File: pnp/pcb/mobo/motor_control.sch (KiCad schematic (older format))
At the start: 48 parts, among them J1 X_MOTOR, J2 Y_MOTOR1, J3 Z_MOTOR, J37 P_MOTOR, J38 C_MOTOR, J4 R_MOTOR, J48 Y_MOTOR2

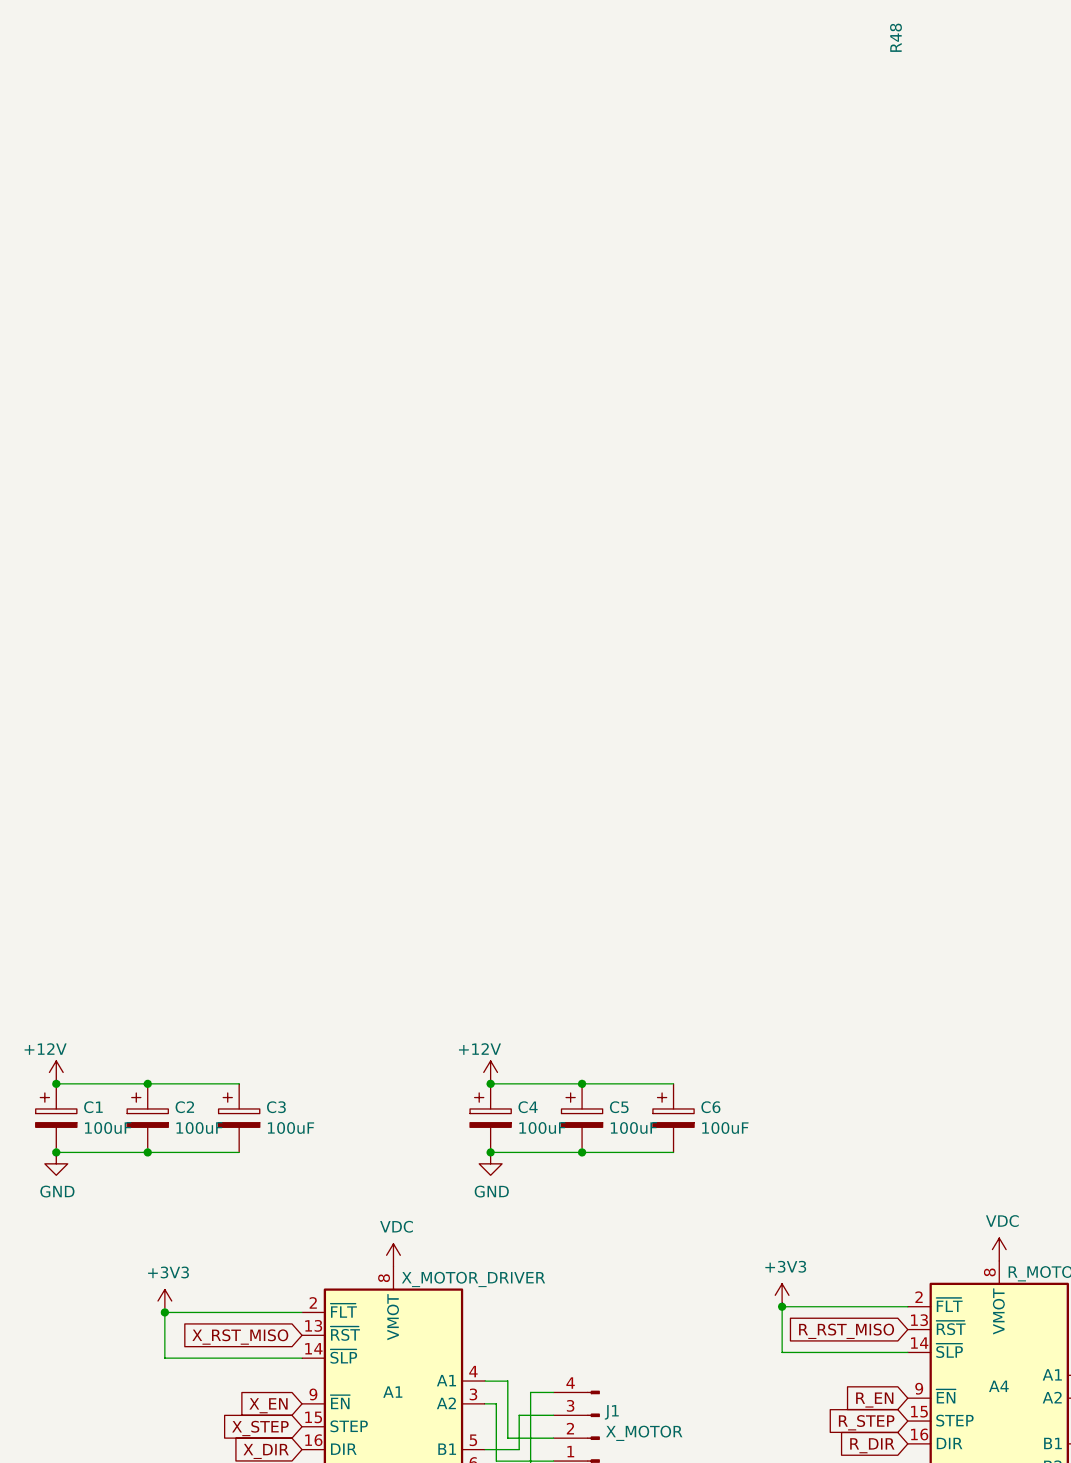
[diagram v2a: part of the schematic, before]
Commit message: Replace MOSFETs and organized vacuum sensor
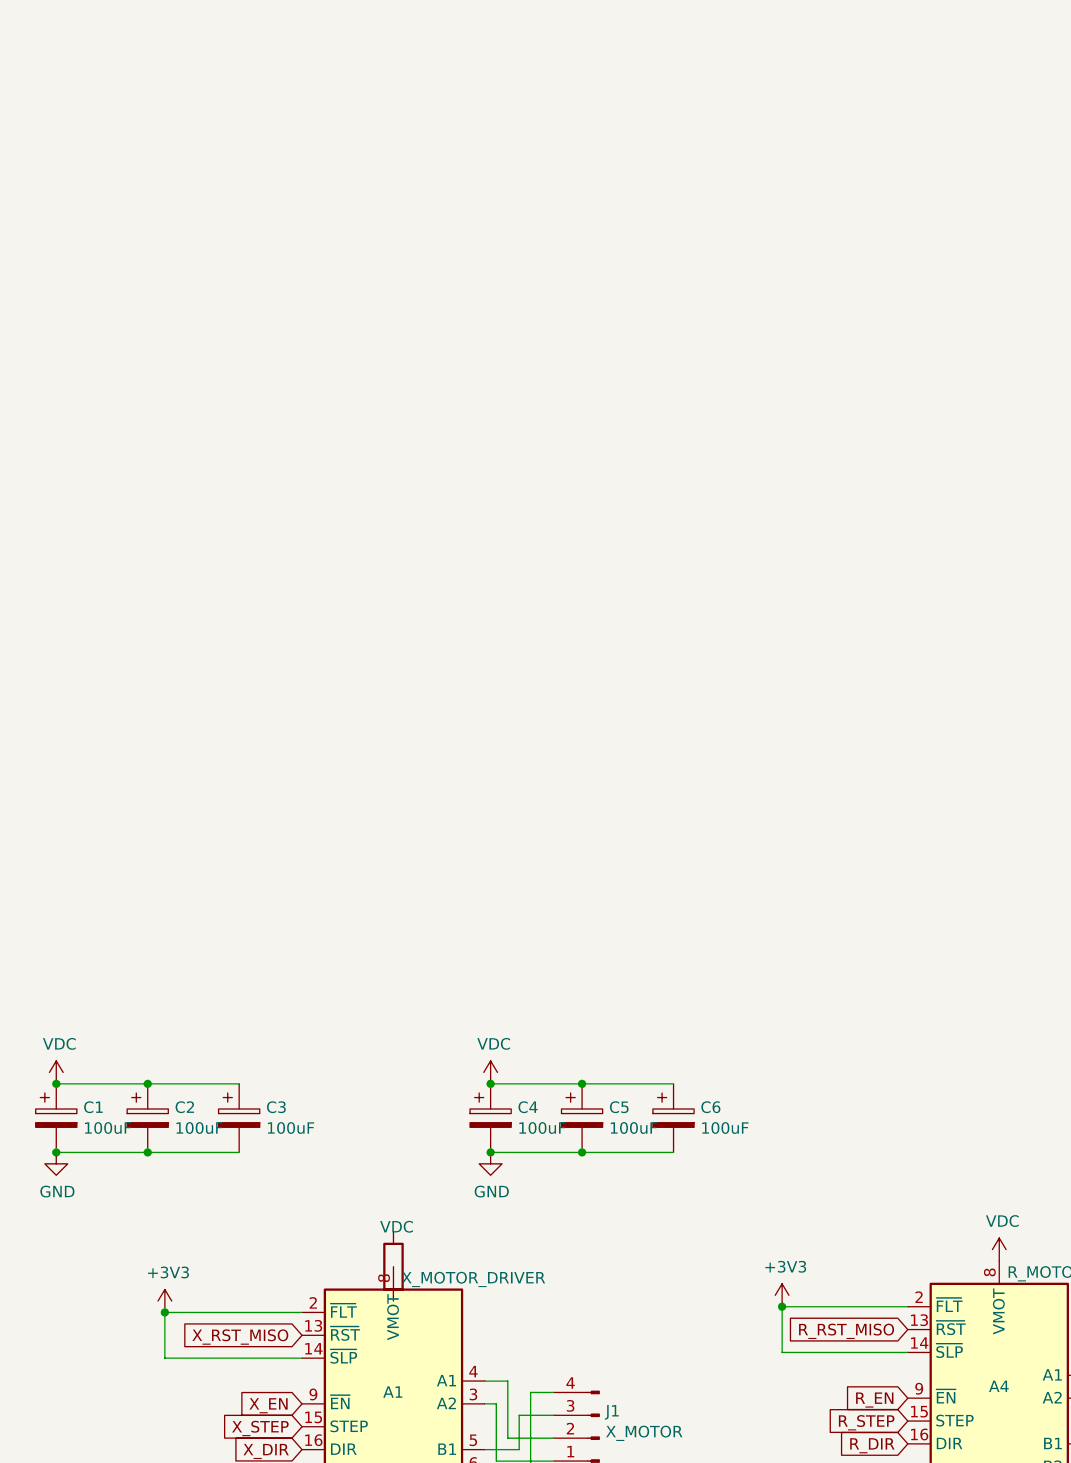
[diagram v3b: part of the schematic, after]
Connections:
- net +12V is gone; now on net VDC: C1.1, C2.1, C3.1, C4.1, C5.1, C6.1
- net VDC: no longer A1.8 (VMOT)
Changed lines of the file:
@@
 $Descr A4 11693 8268
 encoding utf-8
-Sheet 2 6
+Sheet 2 8
 Title ""
 Date ""
@@
 $EndComp
 $Comp
-L power:+12V #PWR0110
-U 1 1 5E43652E
-P 750 750
-F 0 "#PWR0110" H 750 600 50  0001 C CNN
-F 1 "+12V" H 700 900 50  0000 C CNN
-F 2 "" H 750 750 50  0001 C CNN
-F 3 "" H 750 750 50  0001 C CNN
-	1    750  750
-	1    0    0    -1
-$EndComp
-$Comp
 L power:GND #PWR0111
 U 1 1 5E436D6B
@@
 	1150 750  750  750
 Connection ~ 1150 750
-Connection ~ 750  750
 Wire Wire Line
 	1550 1050 1150 1050
@@
 $EndComp
 $Comp
-L power:+12V #PWR0219
-U 1 1 5EB7819A
-P 2650 750
-F 0 "#PWR0219" H 2650 600 50  0001 C CNN
-F 1 "+12V" H 2600 900 50  0000 C CNN
-F 2 "" H 2650 750 50  0001 C CNN
-F 3 "" H 2650 750 50  0001 C CNN
-	1    2650 750
-	1    0    0    -1
-$EndComp
-$Comp
 L power:GND #PWR0220
 U 1 1 5EB781A0
@@
 	3050 750  2650 750
 Connection ~ 3050 750
-Connection ~ 2650 750
 Wire Wire Line
 	3450 1050 3050 1050
@@
 $EndComp
 $Comp
-L Device:R R48
-U 1 1 5FEA9C63
-P 4325 6925
-F 0 "R48" V 4425 6925 50  0000 C CNN
-F 1 "1k" V 4525 6925 50  0000 C CNN
-F 2 "Resistor_SMD:R_0805_2012Metric_Pad1.20x1.40mm_HandSolder" V 4255 6925 50  0001 C CNN
-F 3 "~" H 4325 6925 50  0001 C CNN
-	1    4325 6925
-	0    1    1    0
-$Comp
-L power:VDC #PWR03
+L Device:R #PWR3
 U 1 1 5FE11833
 P 2225 1550
-F 0 "#PWR03" H 2225 1450 50  0001 C CNN
+F 0 "#PWR3" H 2225 1450 50  0001 C CNN
 F 1 "VDC" H 2240 1723 50  0000 C CNN
 F 2 "" H 2225 1550 50  0001 C CNN
@@
 	1    0    0    -1
 $EndComp
+$Comp
+L power:VDC #PWR0102
+U 1 1 5FEE6C11
+P 2650 750
+F 0 "#PWR0102" H 2650 650 50  0001 C CNN
+F 1 "VDC" H 2665 923 50  0000 C CNN
+F 2 "" H 2650 750 50  0001 C CNN
+F 3 "" H 2650 750 50  0001 C CNN
+	1    2650 750
+	1    0    0    -1
+$EndComp
+Connection ~ 2650 750
+$Comp
+L power:VDC #PWR0104
+U 1 1 5FEE782B
+P 750 750
+F 0 "#PWR0104" H 750 650 50  0001 C CNN
+F 1 "VDC" H 765 923 50  0000 C CNN
+F 2 "" H 750 750 50  0001 C CNN
+F 3 "" H 750 750 50  0001 C CNN
+	1    750  750
+	1    0    0    -1
+$EndComp
+Connection ~ 750  750
 $EndSCHEMATC

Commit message: Revert "Replace MOSFETs and organized vacuum sensor"
This reverts commit d845c98ea56ba571b636da2743323a7f663cddfe.
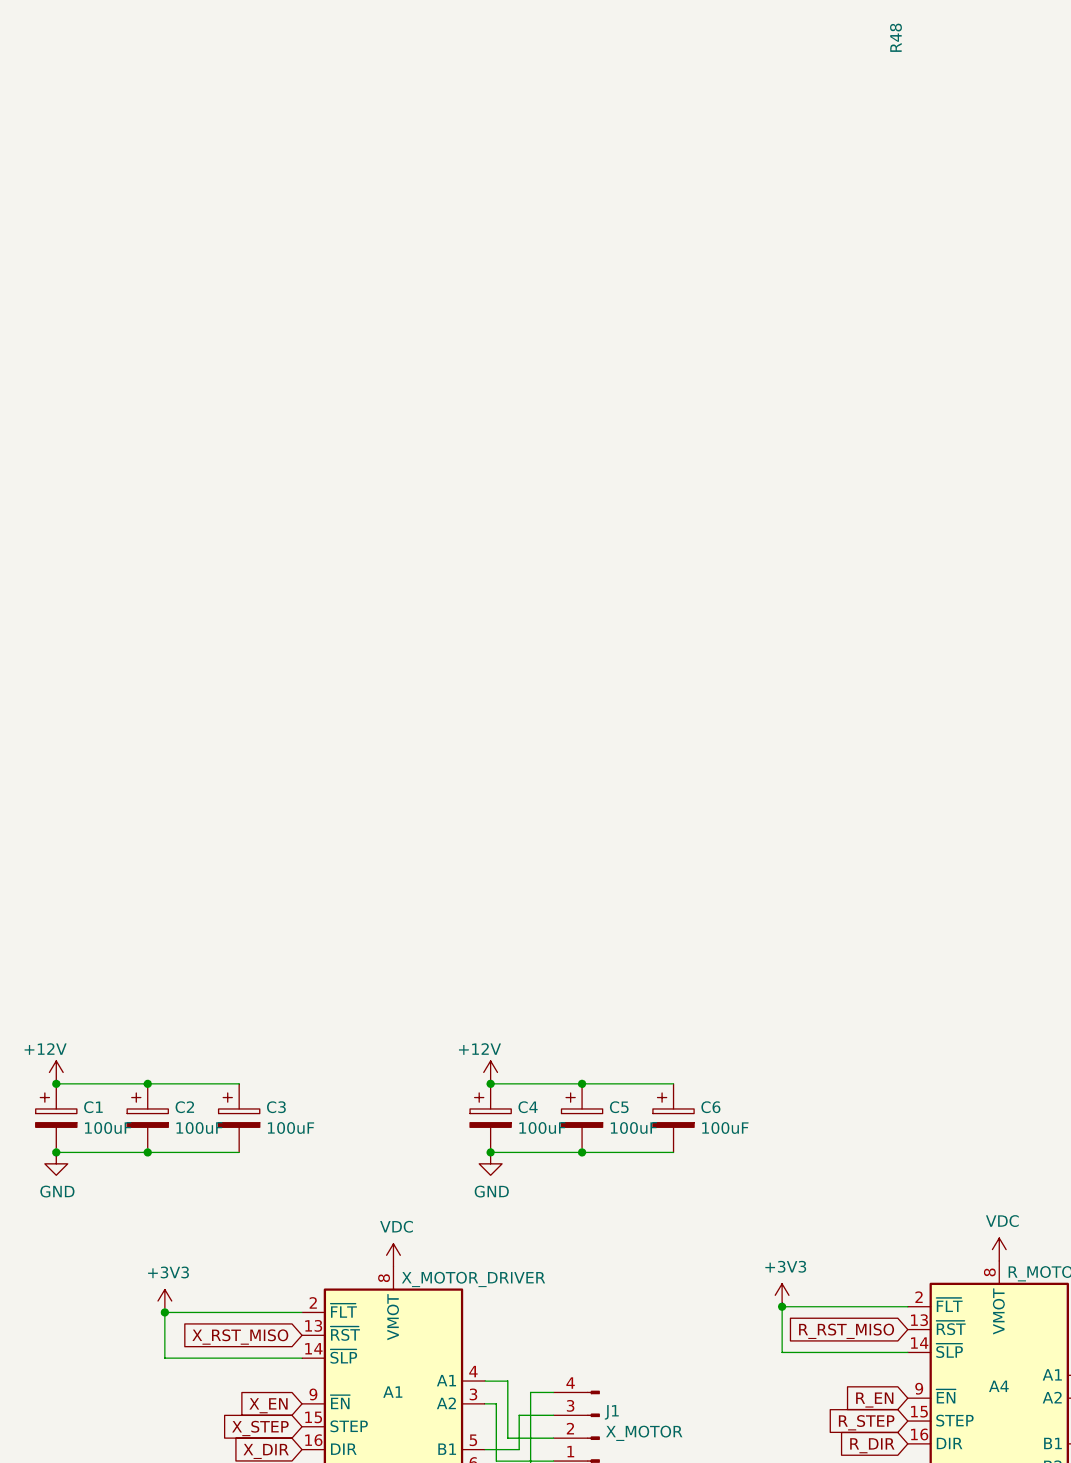
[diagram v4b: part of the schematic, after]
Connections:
- net VDC: now also A1.8 (VMOT); no longer C1.1, C2.1, C3.1, C4.1, C5.1, C6.1
- new net +12V: C1.1, C2.1, C3.1, C4.1, C5.1, C6.1
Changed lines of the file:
@@
 $Descr A4 11693 8268
 encoding utf-8
-Sheet 2 8
+Sheet 2 6
 Title ""
 Date ""
@@
 $EndComp
 $Comp
+L power:+12V #PWR0110
+U 1 1 5E43652E
+P 750 750
+F 0 "#PWR0110" H 750 600 50  0001 C CNN
+F 1 "+12V" H 700 900 50  0000 C CNN
+F 2 "" H 750 750 50  0001 C CNN
+F 3 "" H 750 750 50  0001 C CNN
+	1    750  750
+	1    0    0    -1
+$EndComp
+$Comp
 L power:GND #PWR0111
 U 1 1 5E436D6B
@@
 	1150 750  750  750
 Connection ~ 1150 750
+Connection ~ 750  750
 Wire Wire Line
 	1550 1050 1150 1050
@@
 $EndComp
 $Comp
+L power:+12V #PWR0219
+U 1 1 5EB7819A
+P 2650 750
+F 0 "#PWR0219" H 2650 600 50  0001 C CNN
+F 1 "+12V" H 2600 900 50  0000 C CNN
+F 2 "" H 2650 750 50  0001 C CNN
+F 3 "" H 2650 750 50  0001 C CNN
+	1    2650 750
+	1    0    0    -1
+$EndComp
+$Comp
 L power:GND #PWR0220
 U 1 1 5EB781A0
@@
 	3050 750  2650 750
 Connection ~ 3050 750
+Connection ~ 2650 750
 Wire Wire Line
 	3450 1050 3050 1050
@@
 $EndComp
 $Comp
-L Device:R #PWR3
+L Device:R R48
+U 1 1 5FEA9C63
+P 4325 6925
+F 0 "R48" V 4425 6925 50  0000 C CNN
+F 1 "1k" V 4525 6925 50  0000 C CNN
+F 2 "Resistor_SMD:R_0805_2012Metric_Pad1.20x1.40mm_HandSolder" V 4255 6925 50  0001 C CNN
+F 3 "~" H 4325 6925 50  0001 C CNN
+	1    4325 6925
+	0    1    1    0
+$Comp
+L power:VDC #PWR03
 U 1 1 5FE11833
 P 2225 1550
-F 0 "#PWR3" H 2225 1450 50  0001 C CNN
+F 0 "#PWR03" H 2225 1450 50  0001 C CNN
 F 1 "VDC" H 2240 1723 50  0000 C CNN
 F 2 "" H 2225 1550 50  0001 C CNN
@@
 	1    0    0    -1
 $EndComp
-$Comp
-L power:VDC #PWR0102
-U 1 1 5FEE6C11
-P 2650 750
-F 0 "#PWR0102" H 2650 650 50  0001 C CNN
-F 1 "VDC" H 2665 923 50  0000 C CNN
-F 2 "" H 2650 750 50  0001 C CNN
-F 3 "" H 2650 750 50  0001 C CNN
-	1    2650 750
-	1    0    0    -1
-$EndComp
-Connection ~ 2650 750
-$Comp
-L power:VDC #PWR0104
-U 1 1 5FEE782B
-P 750 750
-F 0 "#PWR0104" H 750 650 50  0001 C CNN
-F 1 "VDC" H 765 923 50  0000 C CNN
-F 2 "" H 750 750 50  0001 C CNN
-F 3 "" H 750 750 50  0001 C CNN
-	1    750  750
-	1    0    0    -1
-$EndComp
-Connection ~ 750  750
 $EndSCHEMATC

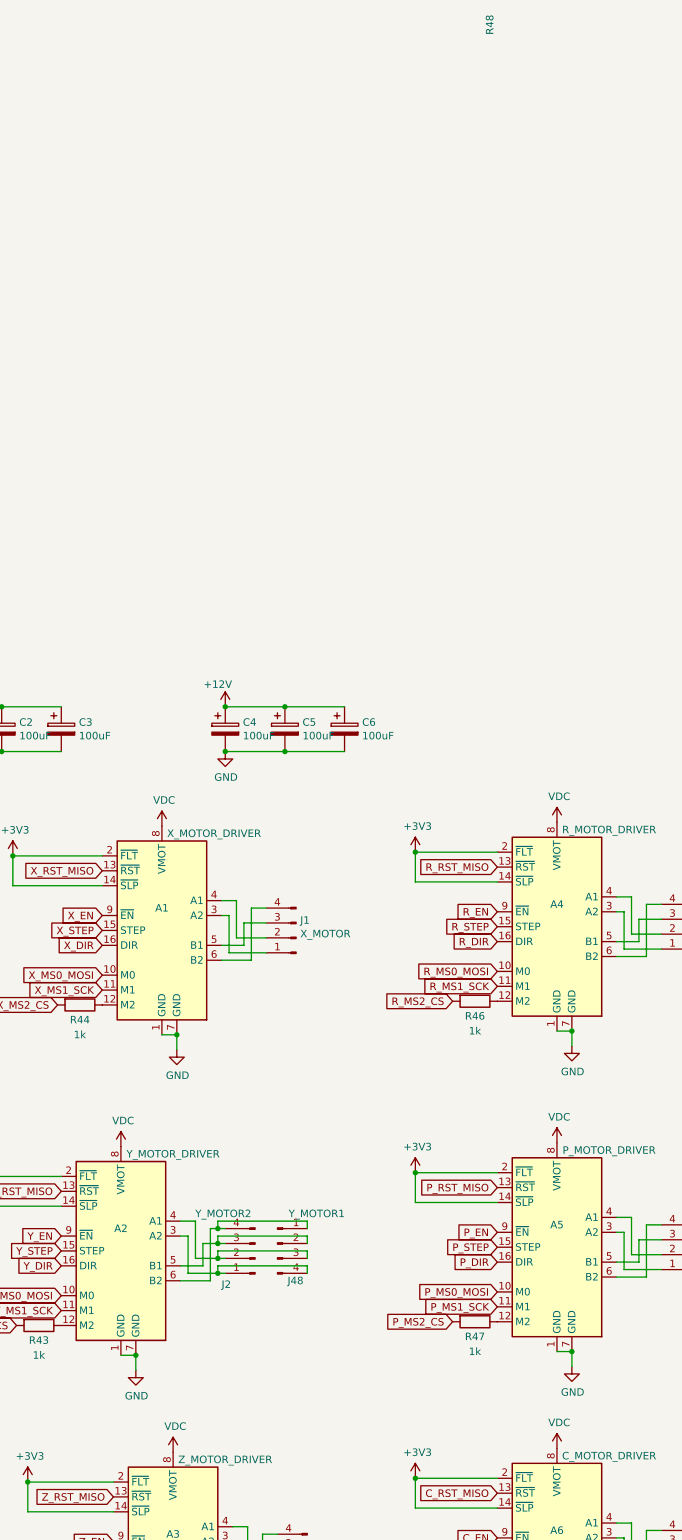
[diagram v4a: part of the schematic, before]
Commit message: Revert 24V support, only routing is left
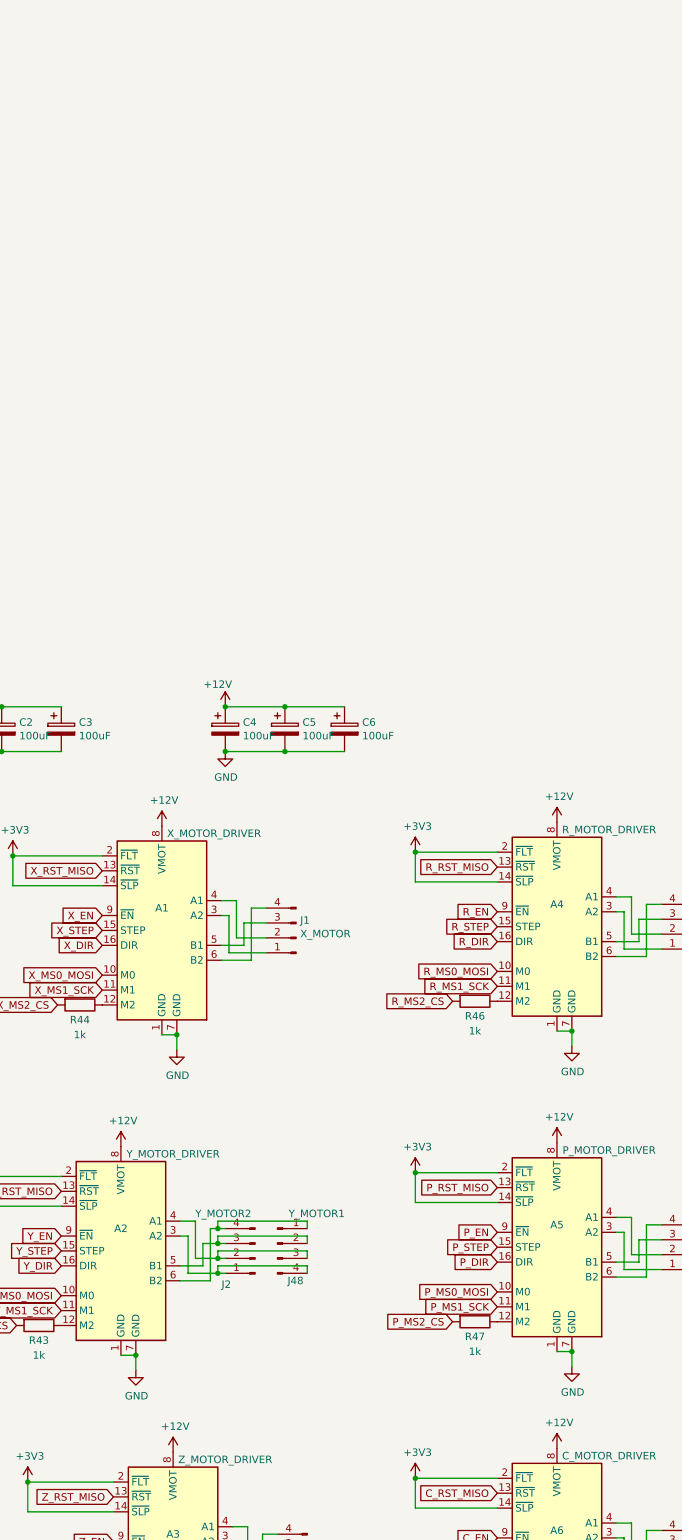
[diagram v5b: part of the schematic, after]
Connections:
- net VDC is gone; now on net +12V: A1.8 (VMOT), A2.8 (VMOT), A3.8 (VMOT), A4.8 (VMOT), A5.8 (VMOT), A6.8 (VMOT)
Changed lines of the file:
@@
 $EndComp
 $Comp
-L Device:R R48
-U 1 1 5FEA9C63
-P 4325 6925
-F 0 "R48" V 4425 6925 50  0000 C CNN
-F 1 "1k" V 4525 6925 50  0000 C CNN
-F 2 "Resistor_SMD:R_0805_2012Metric_Pad1.20x1.40mm_HandSolder" V 4255 6925 50  0001 C CNN
-F 3 "~" H 4325 6925 50  0001 C CNN
-	1    4325 6925
-	0    1    1    0
-$Comp
-L power:VDC #PWR03
-U 1 1 5FE11833
+L power:+12V #PWR0106
+U 1 1 5FF1A1A9
 P 2225 1550
-F 0 "#PWR03" H 2225 1450 50  0001 C CNN
-F 1 "VDC" H 2240 1723 50  0000 C CNN
+F 0 "#PWR0106" H 2225 1400 50  0001 C CNN
+F 1 "+12V" H 2240 1723 50  0000 C CNN
 F 2 "" H 2225 1550 50  0001 C CNN
 F 3 "" H 2225 1550 50  0001 C CNN
@@
 $EndComp
 $Comp
-L power:VDC #PWR06
-U 1 1 5FE12359
+L power:+12V #PWR0131
+U 1 1 5FF1DFBE
 P 4875 1525
-F 0 "#PWR06" H 4875 1425 50  0001 C CNN
-F 1 "VDC" H 4890 1698 50  0000 C CNN
+F 0 "#PWR0131" H 4875 1375 50  0001 C CNN
+F 1 "+12V" H 4890 1698 50  0000 C CNN
 F 2 "" H 4875 1525 50  0001 C CNN
 F 3 "" H 4875 1525 50  0001 C CNN
@@
 $EndComp
 $Comp
-L power:VDC #PWR07
-U 1 1 5FE163D9
+L power:+12V #PWR0133
+U 1 1 5FF1FEB6
+P 1950 3700
+F 0 "#PWR0133" H 1950 3550 50  0001 C CNN
+F 1 "+12V" H 1965 3873 50  0000 C CNN
+F 2 "" H 1950 3700 50  0001 C CNN
+F 3 "" H 1950 3700 50  0001 C CNN
+	1    1950 3700
+	1    0    0    -1
+$EndComp
+$Comp
+L power:+12V #PWR0134
+U 1 1 5FF2076D
 P 4875 3675
-F 0 "#PWR07" H 4875 3575 50  0001 C CNN
-F 1 "VDC" H 4890 3848 50  0000 C CNN
+F 0 "#PWR0134" H 4875 3525 50  0001 C CNN
+F 1 "+12V" H 4890 3848 50  0000 C CNN
 F 2 "" H 4875 3675 50  0001 C CNN
 F 3 "" H 4875 3675 50  0001 C CNN
@@
 $EndComp
 $Comp
-L power:VDC #PWR08
-U 1 1 5FE16DA3
-P 4875 5725
-F 0 "#PWR08" H 4875 5625 50  0001 C CNN
-F 1 "VDC" H 4890 5898 50  0000 C CNN
-F 2 "" H 4875 5725 50  0001 C CNN
-F 3 "" H 4875 5725 50  0001 C CNN
-	1    4875 5725
-	1    0    0    -1
-$EndComp
-$Comp
-L power:VDC #PWR05
-U 1 1 5FE1767F
+L power:+12V #PWR0136
+U 1 1 5FF26940
 P 2300 5750
-F 0 "#PWR05" H 2300 5650 50  0001 C CNN
-F 1 "VDC" H 2315 5923 50  0000 C CNN
+F 0 "#PWR0136" H 2300 5600 50  0001 C CNN
+F 1 "+12V" H 2315 5923 50  0000 C CNN
 F 2 "" H 2300 5750 50  0001 C CNN
 F 3 "" H 2300 5750 50  0001 C CNN
@@
 $EndComp
 $Comp
-L power:VDC #PWR01
-U 1 1 5FE1815F
-P 1950 3700
-F 0 "#PWR01" H 1950 3600 50  0001 C CNN
-F 1 "VDC" H 1965 3873 50  0000 C CNN
-F 2 "" H 1950 3700 50  0001 C CNN
-F 3 "" H 1950 3700 50  0001 C CNN
-	1    1950 3700
+L power:+12V #PWR0137
+U 1 1 5FF27268
+P 4875 5725
+F 0 "#PWR0137" H 4875 5575 50  0001 C CNN
+F 1 "+12V" H 4890 5898 50  0000 C CNN
+F 2 "" H 4875 5725 50  0001 C CNN
+F 3 "" H 4875 5725 50  0001 C CNN
+	1    4875 5725
 	1    0    0    -1
 $EndComp
